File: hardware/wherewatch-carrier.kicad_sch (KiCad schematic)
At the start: 24 parts, among them J1 LiPo JST PH, J3 u.FL GNSS antenna, J4 vibration motor, J5 speaker 4R, J6 OLED 0.42in I2C, Q3 2N7002, SW1 MSK-12C02, SW2 TS-1187A, U1 XIAO ESP32S3 Sense, U2 LSM6DS3TR-C, U3 ATGM336H-5N31, U4 MAX98357A

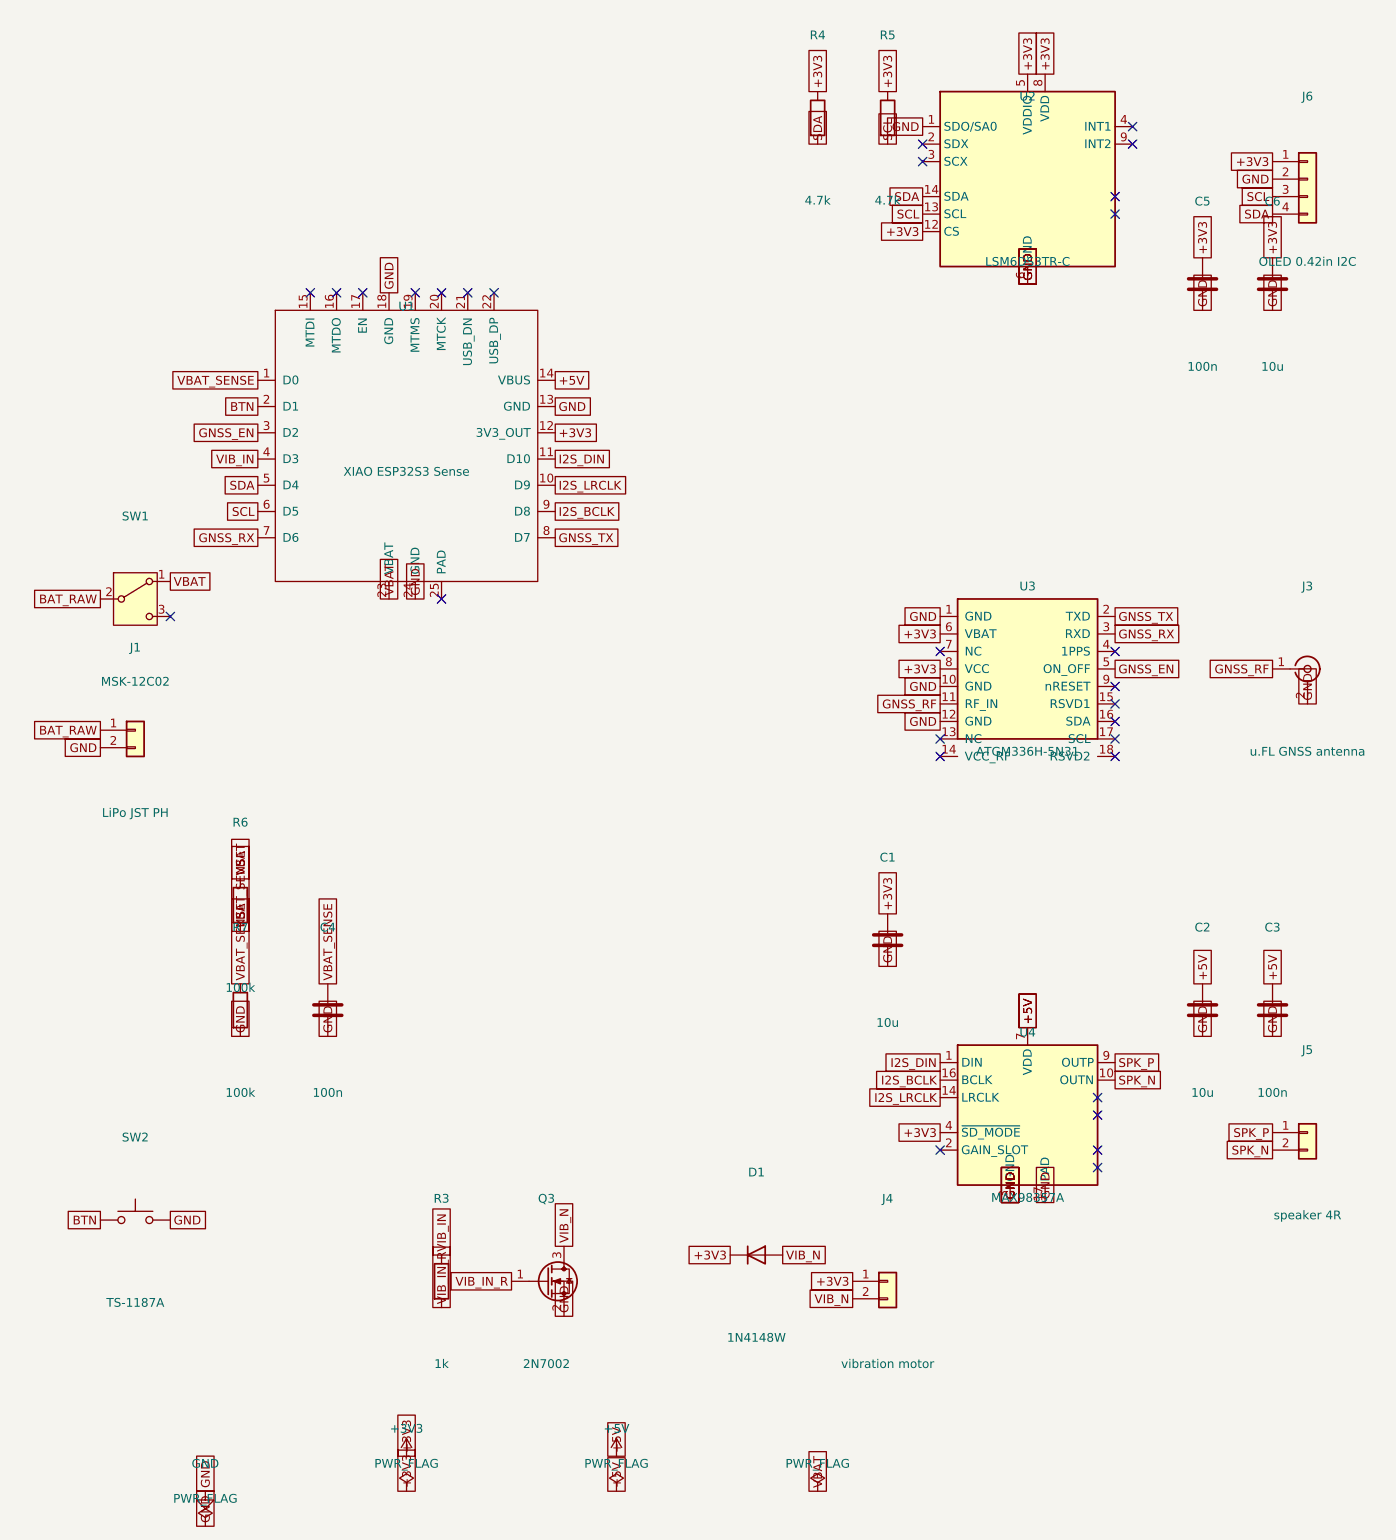
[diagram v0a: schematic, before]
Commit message: hardware: v0.2 after review: amp on VBAT, antenna bias-T, ON/OFF and gate pulldowns
Review findings from claudeMB (19:06Z) and codexmb (19:07Z), both accepted:
- MAX98357A VDD and its caps move from +5V (USB VBUS only) to VBAT after
  the slide switch, so the speaker works on the cell and its peaks stay
  off the XIAO's 700 mA 3V3 regulator. +5V no longer exists on the carrier.
- GNSS antenna: the ATGM336H manual's active-antenna circuit, VCC_RF
  (pin 14) through a 47 nH inductor onto the antenna line; the antenna
  becomes an active ceramic patch on u.FL. The passive+AT2659 path is the
  documented alternative if an active patch does not fit the case.
- 100 k pulldowns on the vibration driver gate (no twitch at boot) and on
  the GNSS ON/OFF line (GNSS held off through reset).

ERC: 0 errors, the same 4 accepted warnings. Exports regenerated.

Co-Authored-By: Claude Fable 5.1 <noreply@anthropic.com>
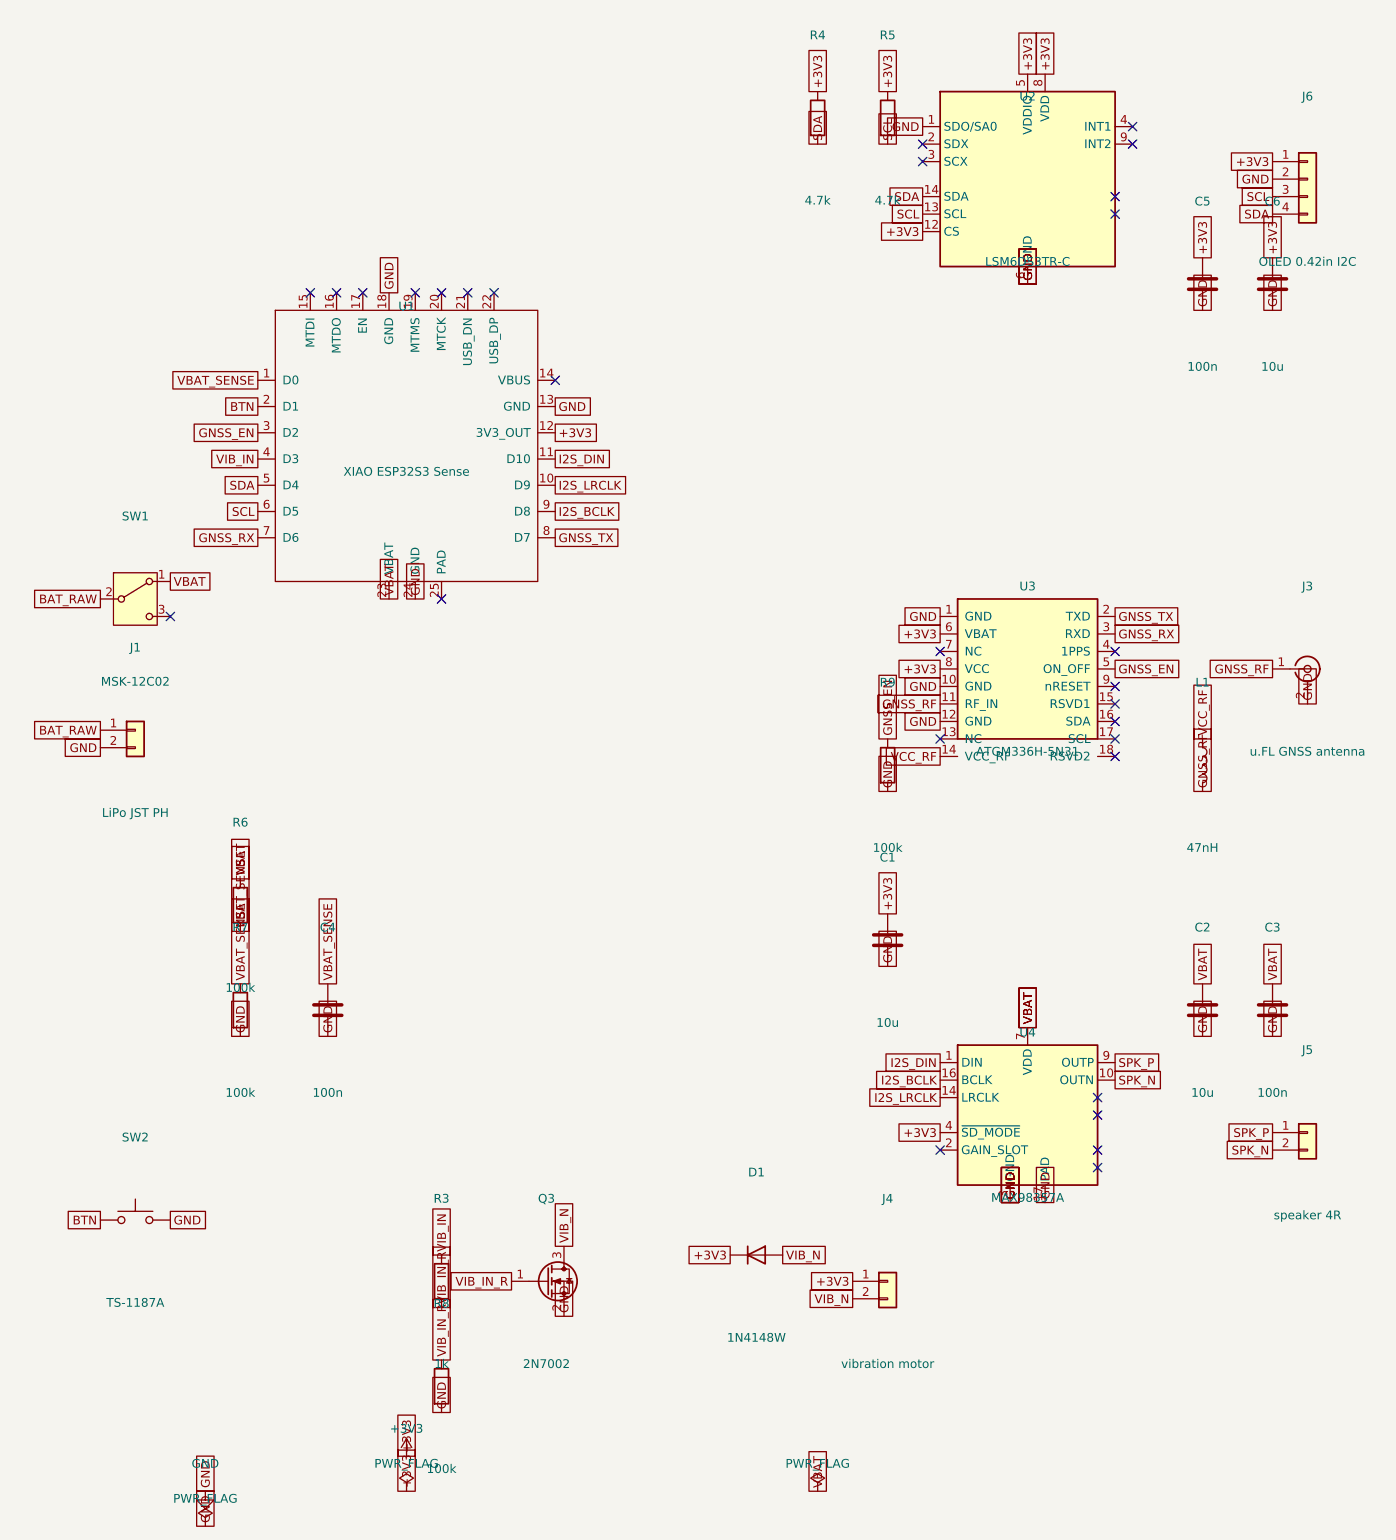
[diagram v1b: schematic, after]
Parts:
- added L1: 47nH, Inductor_SMD:L_0402_1005Metric, symbol Device:L
- added R8, R9: 100k, Resistor_SMD:R_0402_1005Metric, symbol Device:R
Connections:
- net GND: now also R8.2, R9.2
- net GNSS_EN: now also R9.1
- net GNSS_RF: now also L1.2
- net VBAT: now also C2.1, C3.1, U4.7 (VDD), U4.8 (VDD)
- net VIB_IN_R: now also R8.1
- net VCC_RF: now reaches U3.14 (VCC_RF)
- net VCC_RF: now also L1.1
- removed net +5V: C2.1, C3.1, U1.14 (VBUS), U4.7 (VDD), U4.8 (VDD)

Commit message: hardware: v0.2.1, SD_MODE tied to the amp VDD per the datasheet figure; datasheet checks recorded
MAX98357A VIH 1.3 V / VIL 0.6 V absolute (3.3 V I2S on a 4.2 V rail OK);
ATGM336H active-antenna circuit has no external DC block (manual 2.7.1).

Co-Authored-By: Claude Fable 5.1 <noreply@anthropic.com>
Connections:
- net +3V3: no longer U4.4 (~{SD_MODE})
- net VBAT: now also U4.4 (~{SD_MODE})
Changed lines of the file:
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@@
     (effects (font (size 1.27 1.27)) (justify right))
     (property "Intersheetrefs" "${INTERSHEET_REFS}" (at 137.16 170.18 0) (effects (font (size 1.27 1.27)) (hide yes))))
-  (global_label "+3V3" (shape passive) (at 137.16 177.80 180) (fields_autoplaced yes)
+  (global_label "VBAT" (shape passive) (at 137.16 177.80 180) (fields_autoplaced yes)
     (effects (font (size 1.27 1.27)) (justify right))
     (property "Intersheetrefs" "${INTERSHEET_REFS}" (at 137.16 177.80 0) (effects (font (size 1.27 1.27)) (hide yes))))
@@
 )
   (no_connect (at 68.58 55.88))
+  (no_connect (at 81.28 68.58))
+  (no_connect (at 49.53 55.88))
   (no_connect (at 53.34 55.88))
+  (no_connect (at 64.77 55.88))
   (no_connect (at 64.77 100.33))
   (no_connect (at 45.72 55.88))
-  (no_connect (at 49.53 55.88))
   (no_connect (at 60.96 55.88))
-  (no_connect (at 81.28 68.58))
-  (no_connect (at 64.77 55.88))
   (no_connect (at 72.39 55.88))
+  (no_connect (at 165.10 31.75))
+  (no_connect (at 165.10 34.29))
+  (no_connect (at 162.56 41.91))
   (no_connect (at 134.62 36.83))
-  (no_connect (at 165.10 31.75))
-  (no_connect (at 162.56 41.91))
   (no_connect (at 162.56 44.45))
-  (no_connect (at 165.10 34.29))
   (no_connect (at 134.62 34.29))
-  (no_connect (at 162.56 120.65))
   (no_connect (at 162.56 107.95))
+  (no_connect (at 162.56 113.03))
+  (no_connect (at 162.56 118.11))
+  (no_connect (at 162.56 123.19))
   (no_connect (at 137.16 107.95))
   (no_connect (at 137.16 120.65))
+  (no_connect (at 162.56 120.65))
   (no_connect (at 162.56 115.57))
-  (no_connect (at 162.56 118.11))
-  (no_connect (at 162.56 113.03))
-  (no_connect (at 162.56 123.19))
+  (no_connect (at 160.02 175.26))
+  (no_connect (at 160.02 180.34))
   (no_connect (at 160.02 182.88))
-  (no_connect (at 160.02 180.34))
-  (no_connect (at 160.02 175.26))
+  (no_connect (at 160.02 172.72))
   (no_connect (at 137.16 180.34))
-  (no_connect (at 160.02 172.72))
   (no_connect (at 25.40 102.87))
   (sheet_instances (path "/" (page "1")))

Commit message: hardware: v0.3, MOSFET battery switch with USB-present override; IMU SDx/SCx to GND
codexmb second pass (19:16Z): the MSK-12C02 slide switch is rated 12 V /
50 mA and sat in series with the whole battery load and the charge
current. Now the cell reaches the XIAO's B+ through a 4 A P-MOSFET (Q1,
AO3401A) whose gate is pulled up to the cell (off) and pulled low by
the slide switch ("on") or by Q2 (2N7002) whenever USB VBUS is present,
so the cell charges with the switch in either position and "off" without
USB is zero drain. The switch itself carries microamps. LSM6DS3 SDx/SCx
tied to GND per ST table 2 (mode 1). ERC 0 errors; the extra warnings
are the same accepted classes on the new parts.

Co-Authored-By: Claude Fable 5.1 <noreply@anthropic.com>
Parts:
- added Q1: AO3401A, Package_TO_SOT_SMD:SOT-23, symbol Transistor_FET:AO3401A
- added Q2: 2N7002, Package_TO_SOT_SMD:SOT-23, symbol Transistor_FET:2N7002
- added R1, R10: 100k, Resistor_SMD:R_0402_1005Metric, symbol Device:R
- added R2: 10k, Resistor_SMD:R_0402_1005Metric, symbol Device:R
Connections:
- net BAT_RAW: now also Q1.2 (S), R1.1; no longer SW1.2 (B)
- net GND: now also SW1.2 (B), U2.2 (SDX), U2.3 (SCX), Q2.2 (S), R10.2
- net VBAT: now also Q1.3 (D); no longer SW1.1 (A)
- net VBUS: now reaches U1.14 (VBUS)
- net VBUS: now also R2.1
- new net SW_G: Q1.1 (G), Q2.3 (D), R1.2, SW1.1 (A)
- new net VBUS_DET: Q2.1 (G), R10.1, R2.2
- no-connect marks 29 -> 26
